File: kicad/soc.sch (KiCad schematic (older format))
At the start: 40 parts, among them J1 Line Out, J2 PS/2 Keyboard, J3 Headphone Out, J4 Line In, P1 LED MATRIX, P2 ALTERA_DE1_GPIO, U1 SSM2603, U2 DS3234

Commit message: start of IO board changes
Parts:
- removed R10, R11: 1k, Resistors_SMD:R_0805_HandSoldering, symbol R
- added D?: PWR, symbol Led_Small
- added P?: IO, symbol CONN_02X04
- added R? (x3): 100K, Resistors_SMD:R_0805_HandSoldering, symbol R
- added R?: 100, Resistors_SMD:R_0805_HandSoldering, symbol R
- added U?: speakjet, symbol speakjet
- C10, C7: footprint Capacitors_ThroughHole:C_Radial_D8_L11.5_P3.5 -> mstock:UWXCAP-6.3mm
- C11, C12, C14, C15: footprint Capacitors_ThroughHole:C_Radial_D5_L6_P2.5 -> mstock:UWXCAP-3mm
- C13, C16, C17, C18: footprint Capacitors_ThroughHole:C_Disc_D3_P2.5 -> Capacitors_SMD:C_0805_HandSoldering
- R3, R6, R7: footprint Resistors_ThroughHole:Resistor_Vertical_RM5mm -> Resistors_SMD:R_0805_HandSoldering
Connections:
- net +3V3: now also R3.1, P?.1 (P1), R?.1, R?.1, R?.1, R?.1, U?.12 (M1), U?.14 (VCC); no longer R3.2
- net GND: now also D?.1 (K), P?.7 (P7), U?.1 (RC1), U?.13 (M0), U?.2 (RC0), U?.3 (E5), U?.4 (E4), U?.5 (Gnd), U?.6 (E3), U?.7 (E2), U?.8 (E1), U?.9 (E0)
- net Kbd_clk: now also J2.5
- net Kbd_data: now also J2.1
- net MISO_33: now also P?.4 (P4)
- net MOSI_33: now also P?.2 (P2)
- net SCLK: now also P?.3 (P3), R?.2
- net SCLK_33: now also P?.6 (P6)
- net SDIN: now also P?.5 (P5), R?.2
- net ~OE: now also R?.2
- net ~RTC_SS: now also P?.8 (P8)
- net MCLK: now reaches P2.31 (IO_A26)
- net MCLK: now also U1.1 (MCLK/XTI)
- net SPEAK: now reaches P2.32 (IO_A27)
- net SPEAK: now also U?.16 (D1)
- net ~RESET: now reaches P2.34 (IO_A29)
- net ~RESET: now also U2.6 (~RST), U?.11 (Reset)
- net at U1.25 (MUTE): now also R3.2; no longer R3.1
- new net: D?.2 (A), R?.2
- new net Serial1_TX: U?.10 (RCX)
- new net Serial1_busy: U?.15 (D2)
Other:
- moved on the sheet: C12, C15, C16, C18, J4, R3

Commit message: more work on new IO board
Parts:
- added R13, R14: 10k, Resistors_SMD:R_0805_HandSoldering, symbol R
- D1: renamed from D?; footprint (none) -> mstock:SM1206POL
- P3: renamed from P?; footprint (none) -> Pin_Headers:Pin_Header_Straight_2x06; symbol CONN_02X04 -> CONN_02X06
- U3: renamed from U?; footprint (none) -> Housings_DIP:DIP-18_W7.62mm
- gave numbers to parts that had none: 4
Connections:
- net Serial1 is gone; now on net Serial1_TX: P2.1 (IO_A0)
- net GND: now also P3.11 (P11); no longer P3.7 (P7)
- net Serial1_TX: now also P3.9 (P9)
- net GPIO1: now reaches P2.33 (IO_A28)
- net GPIO1: now also P3.10 (P10)
- net GPIO2: now reaches P2.35 (IO_A30)
- net GPIO2: now also P3.12 (P12)
- net at U1.16 (LOUT): now also R14.2; no longer C14.1
- net voice: now reaches U3.18 (Voice)
- net voice: now also P3.7 (P7), R13.2
- net SPEAK renamed speaking
- new net: C14.1, R13.1, R14.1
- no-connect marks 10 -> 15
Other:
- moved on the sheet: U3
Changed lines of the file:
@@
 $EndComp
 Text Label 1750 1200 2    60   ~ 0
-Serial1
+Serial1_TX
 $Comp
 L +3.3V #PWR01
@@
 MCLK
 $Comp
-L R R?
+L R R11
 U 1 1 5830728C
 P 3450 4600
-F 0 "R?" V 3243 4600 50  0000 C CNN
+F 0 "R11" V 3243 4600 50  0000 C CNN
 F 1 "100K" V 3334 4600 50  0000 C CNN
 F 2 "Resistors_SMD:R_0805_HandSoldering" V 3380 4600 50  0001 C CNN
@@
 $EndComp
 $Comp
-L R R?
+L R R10
 U 1 1 5830740A
 P 3150 4600
-F 0 "R?" V 2943 4600 50  0000 C CNN
+F 0 "R10" V 2943 4600 50  0000 C CNN
 F 1 "100K" V 3034 4600 50  0000 C CNN
 F 2 "Resistors_SMD:R_0805_HandSoldering" V 3080 4600 50  0001 C CNN
@@
 $EndComp
 $Comp
-L CONN_02X04 P?
+L CONN_02X06 P3
 U 1 1 58308B84
-P 8350 2400
-F 0 "P?" H 8350 2650 50  0000 C CNN
-F 1 "IO" V 8350 2400 50  0000 C CNN
-F 2 "" H 8350 1200 50  0000 C CNN
-F 3 "" H 8350 1200 50  0000 C CNN
-	1    8350 2400
+P 8350 2500
+F 0 "P3" H 8350 2850 50  0000 C CNN
+F 1 "IO" V 8350 2500 50  0000 C CNN
+F 2 "Pin_Headers:Pin_Header_Straight_2x06" H 8350 1300 50  0001 C CNN
+F 3 "" H 8350 1300 50  0000 C CNN
+	1    8350 2500
 	1    0    0    -1
 $EndComp
@@
 ~RTC_SS
 $Comp
-L +3.3V #PWR?
+L +3.3V #PWR021
 U 1 1 583094AC
 P 8100 2150
-F 0 "#PWR?" H 8100 2000 50  0001 C CNN
+F 0 "#PWR021" H 8100 2000 50  0001 C CNN
 F 1 "+3.3V" H 8100 2290 50  0000 C CNN
 F 2 "" H 8100 2150 60  0000 C CNN
@@
 $EndComp
 $Comp
-L GND #PWR?
+L GND #PWR022
 U 1 1 58309716
-P 8100 2650
-F 0 "#PWR?" H 8100 2400 50  0001 C CNN
-F 1 "GND" H 8100 2500 50  0000 C CNN
-F 2 "" H 8100 2650 60  0000 C CNN
-F 3 "" H 8100 2650 60  0000 C CNN
-	1    8100 2650
-	1    0    0    -1
-$EndComp
-$Comp
-L Led_Small D?
+P 8100 2850
+F 0 "#PWR022" H 8100 2600 50  0001 C CNN
+F 1 "GND" H 8100 2700 50  0000 C CNN
+F 2 "" H 8100 2850 60  0000 C CNN
+F 3 "" H 8100 2850 60  0000 C CNN
+	1    8100 2850
+	1    0    0    -1
+$EndComp
+$Comp
+L Led_Small D1
 U 1 1 58309858
 P 9750 2150
-F 0 "D?" H 9750 2385 50  0000 C CNN
+F 0 "D1" H 9750 2385 50  0000 C CNN
 F 1 "PWR" H 9750 2294 50  0000 C CNN
-F 2 "" V 9750 2150 50  0000 C CNN
+F 2 "mstock:SM1206POL" V 9750 2150 50  0001 C CNN
 F 3 "" V 9750 2150 50  0000 C CNN
 	1    9750 2150
@@
 $EndComp
 $Comp
-L +3.3V #PWR?
+L +3.3V #PWR023
 U 1 1 58309B06
 P 10200 2050
-F 0 "#PWR?" H 10200 1900 50  0001 C CNN
+F 0 "#PWR023" H 10200 1900 50  0001 C CNN
 F 1 "+3.3V" H 10200 2190 50  0000 C CNN
 F 2 "" H 10200 2050 60  0000 C CNN
@@
 $EndComp
 $Comp
-L R R?
+L R R15
 U 1 1 58309C0D
 P 10050 2150
-F 0 "R?" V 10130 2150 50  0000 C CNN
+F 0 "R15" V 10130 2150 50  0000 C CNN
 F 1 "100" V 10050 2150 50  0000 C CNN
 F 2 "Resistors_SMD:R_0805_HandSoldering" V 9980 2150 50  0001 C CNN
@@
 $EndComp
 $Comp
-L GND #PWR?
+L GND #PWR024
 U 1 1 58309F9E
 P 9650 2200
-F 0 "#PWR?" H 9650 1950 50  0001 C CNN
+F 0 "#PWR024" H 9650 1950 50  0001 C CNN
 F 1 "GND" H 9650 2050 50  0000 C CNN
 F 2 "" H 9650 2200 60  0000 C CNN
@@
 $EndComp
 $Comp
-L R R?
+L R R12
 U 1 1 5830A3C4
 P 4250 1500
-F 0 "R?" V 4043 1500 50  0000 C CNN
+F 0 "R12" V 4043 1500 50  0000 C CNN
 F 1 "100K" V 4134 1500 50  0000 C CNN
 F 2 "Resistors_SMD:R_0805_HandSoldering" V 4180 1500 50  0001 C CNN
@@
 $EndComp
 $Comp
-L +3.3V #PWR?
+L +3.3V #PWR025
 U 1 1 5830A737
 P 4250 1250
-F 0 "#PWR?" H 4250 1100 50  0001 C CNN
+F 0 "#PWR025" H 4250 1100 50  0001 C CNN
 F 1 "+3.3V" H 4250 1390 50  0000 C CNN
 F 2 "" H 4250 1250 60  0000 C CNN
@@
 $EndComp
 $Comp
-L speakjet U?
+L speakjet U3
 U 1 1 583237DA
-P 3400 6700
-F 0 "U?" H 3425 7347 60  0000 C CNN
-F 1 "speakjet" H 3425 7241 60  0000 C CNN
-F 2 "" H 3450 6650 60  0000 C CNN
-F 3 "" H 3450 6650 60  0000 C CNN
-	1    3400 6700
-	1    0    0    -1
-$EndComp
-$Comp
-L GND #PWR?
+P 1550 4300
+F 0 "U3" H 1575 4947 60  0000 C CNN
+F 1 "speakjet" H 1575 4841 60  0000 C CNN
+F 2 "Housings_DIP:DIP-18_W7.62mm" H 1600 4250 60  0001 C CNN
+F 3 "" H 1600 4250 60  0000 C CNN
+	1    1550 4300
+	1    0    0    -1
+$EndComp
+$Comp
+L GND #PWR026
 U 1 1 583239A7
-P 2900 7200
-F 0 "#PWR?" H 2900 6950 50  0001 C CNN
-F 1 "GND" H 2900 7050 50  0000 C CNN
-F 2 "" H 2900 7200 60  0000 C CNN
-F 3 "" H 2900 7200 60  0000 C CNN
-	1    2900 7200
+P 1050 4800
+F 0 "#PWR026" H 1050 4550 50  0001 C CNN
+F 1 "GND" H 1050 4650 50  0000 C CNN
+F 2 "" H 1050 4800 60  0000 C CNN
+F 3 "" H 1050 4800 60  0000 C CNN
+	1    1050 4800
 	1    0    0    -1
 $EndComp
@@
 Connection ~ 8600 4300
 Wire Wire Line
-	7950 4100 6250 4100
-Wire Wire Line
-	6250 4100 6250 4150
-Wire Wire Line
-	6250 4150 5550 4150
+	5550 4150 6450 4150
 Wire Wire Line
 	5800 4300 7550 4300
@@
 	8100 2150 8100 2250
 Wire Wire Line
-	8100 2550 8100 2650
-Wire Wire Line
 	10200 2050 10200 2150
 Wire Wire Line
@@
 	4250 1250 4250 1350
 Wire Wire Line
-	2950 7100 2900 7100
-Wire Wire Line
-	2900 6300 2900 7200
-Wire Wire Line
-	2950 7000 2900 7000
-Connection ~ 2900 7100
-Wire Wire Line
-	2950 6900 2900 6900
-Connection ~ 2900 7000
-Wire Wire Line
-	2950 6800 2900 6800
-Connection ~ 2900 6900
-Wire Wire Line
-	2950 6700 2900 6700
-Connection ~ 2900 6800
-Wire Wire Line
-	2950 6300 2900 6300
-Connection ~ 2900 6700
-Wire Wire Line
-	2950 6600 2900 6600
-Connection ~ 2900 6600
-Wire Wire Line
-	2950 6500 2900 6500
-Connection ~ 2900 6500
-Wire Wire Line
-	2950 6400 2900 6400
-Connection ~ 2900 6400
-Text Label 3900 7100 0    60   ~ 0
+	1100 4700 1050 4700
+Wire Wire Line
+	1050 3900 1050 4800
+Wire Wire Line
+	1100 4600 1050 4600
+Connection ~ 1050 4700
+Wire Wire Line
+	1100 4500 1050 4500
+Connection ~ 1050 4600
+Wire Wire Line
+	1100 4400 1050 4400
+Connection ~ 1050 4500
+Wire Wire Line
+	1100 4300 1050 4300
+Connection ~ 1050 4400
+Wire Wire Line
+	1100 3900 1050 3900
+Connection ~ 1050 4300
+Wire Wire Line
+	1100 4200 1050 4200
+Connection ~ 1050 4200
+Wire Wire Line
+	1100 4100 1050 4100
+Connection ~ 1050 4100
+Wire Wire Line
+	1100 4000 1050 4000
+Connection ~ 1050 4000
+Text Label 2050 4700 0    60   ~ 0
 Serial1_TX
 $Comp
-L +3.3V #PWR?
+L +3.3V #PWR027
 U 1 1 58324642
-P 4500 6400
-F 0 "#PWR?" H 4500 6250 50  0001 C CNN
-F 1 "+3.3V" H 4500 6540 50  0000 C CNN
-F 2 "" H 4500 6400 60  0000 C CNN
-F 3 "" H 4500 6400 60  0000 C CNN
-	1    4500 6400
-	1    0    0    -1
-$EndComp
-Wire Wire Line
-	3900 6900 4500 6900
-$Comp
-L GND #PWR?
+P 2650 4000
+F 0 "#PWR027" H 2650 3850 50  0001 C CNN
+F 1 "+3.3V" H 2650 4140 50  0000 C CNN
+F 2 "" H 2650 4000 60  0000 C CNN
+F 3 "" H 2650 4000 60  0000 C CNN
+	1    2650 4000
+	1    0    0    -1
+$EndComp
+Wire Wire Line
+	2050 4500 2650 4500
+$Comp
+L GND #PWR028
 U 1 1 58324B78
-P 4450 7200
-F 0 "#PWR?" H 4450 6950 50  0001 C CNN
-F 1 "GND" H 4450 7050 50  0000 C CNN
-F 2 "" H 4450 7200 60  0000 C CNN
-F 3 "" H 4450 7200 60  0000 C CNN
-	1    4450 7200
-	1    0    0    -1
-$EndComp
-Wire Wire Line
-	3900 6800 4450 6800
-Text Label 2750 2700 0    60   ~ 0
-SPEAK
-Text Label 3900 6500 0    60   ~ 0
-SPEAK
-Wire Wire Line
-	3900 6700 4500 6700
+P 2600 4800
+F 0 "#PWR028" H 2600 4550 50  0001 C CNN
+F 1 "GND" H 2600 4650 50  0000 C CNN
+F 2 "" H 2600 4800 60  0000 C CNN
+F 3 "" H 2600 4800 60  0000 C CNN
+	1    2600 4800
+	1    0    0    -1
+$EndComp
+Wire Wire Line
+	2050 4400 2600 4400
+Text Label 2050 4100 0    60   ~ 0
+speaking
+Wire Wire Line
+	2050 4300 2650 4300
 Text Label 2750 2800 0    60   ~ 0
 ~RESET
-Text Label 3900 7000 0    60   ~ 0
+Text Label 2050 4600 0    60   ~ 0
 ~RESET
 Text Label 6100 1400 2    60   ~ 0
 ~RESET
-NoConn ~ 3900 6400
-Wire Wire Line
-	4450 6800 4450 7200
-Text Label 3900 6600 0    60   ~ 0
+NoConn ~ 2050 4000
+Wire Wire Line
+	2600 4400 2600 4800
+Text Label 2050 4200 0    60   ~ 0
 Serial1_busy
 Wire Wire Line
-	4500 6900 4500 6400
-Connection ~ 4500 6700
+	2650 4500 2650 4000
+Connection ~ 2650 4300
+Text Label 2750 2700 0    60   ~ 0
+speaking
+Text Label 2050 3900 0    60   ~ 0
+voice
+Text Label 6450 3800 2    60   ~ 0
+voice
+$Comp
+L R R13
+U 1 1 583306F5
+P 6600 3800
+F 0 "R13" V 6680 3800 50  0000 C CNN
+F 1 "10k" V 6600 3800 50  0000 C CNN
+F 2 "Resistors_SMD:R_0805_HandSoldering" V 6530 3800 50  0001 C CNN
+F 3 "" H 6600 3800 50  0000 C CNN
+	1    6600 3800
+	0    1    1    0
+$EndComp
+$Comp
+L R R14
+U 1 1 583307D9
+P 6600 4100
+F 0 "R14" V 6680 4100 50  0000 C CNN
+F 1 "10k" V 6600 4100 50  0000 C CNN
+F 2 "Resistors_SMD:R_0805_HandSoldering" V 6530 4100 50  0001 C CNN
+F 3 "" H 6600 4100 50  0000 C CNN
+	1    6600 4100
+	0    1    1    0
+$EndComp
+Wire Wire Line
+	6450 4150 6450 4100
+Wire Wire Line
+	6750 3800 6750 4100
+Wire Wire Line
+	6750 4100 7950 4100
+Connection ~ 6750 4100
+Wire Wire Line
+	8100 2750 8100 2850
+Text Label 8100 2550 2    60   ~ 0
+voice
+Text Label 8100 2650 2    60   ~ 0
+Serial1_TX
+Text Label 1750 2800 2    60   ~ 0
+GPIO1
+Text Label 1750 2900 2    60   ~ 0
+GPIO2
+Text Label 8600 2750 0    60   ~ 0
+GPIO2
+Text Label 8600 2650 0    60   ~ 0
+GPIO1
+NoConn ~ 2750 2900
+NoConn ~ 2750 3000
+NoConn ~ 2750 3100
+NoConn ~ 1750 3000
+NoConn ~ 1750 3100
 $EndSCHEMATC

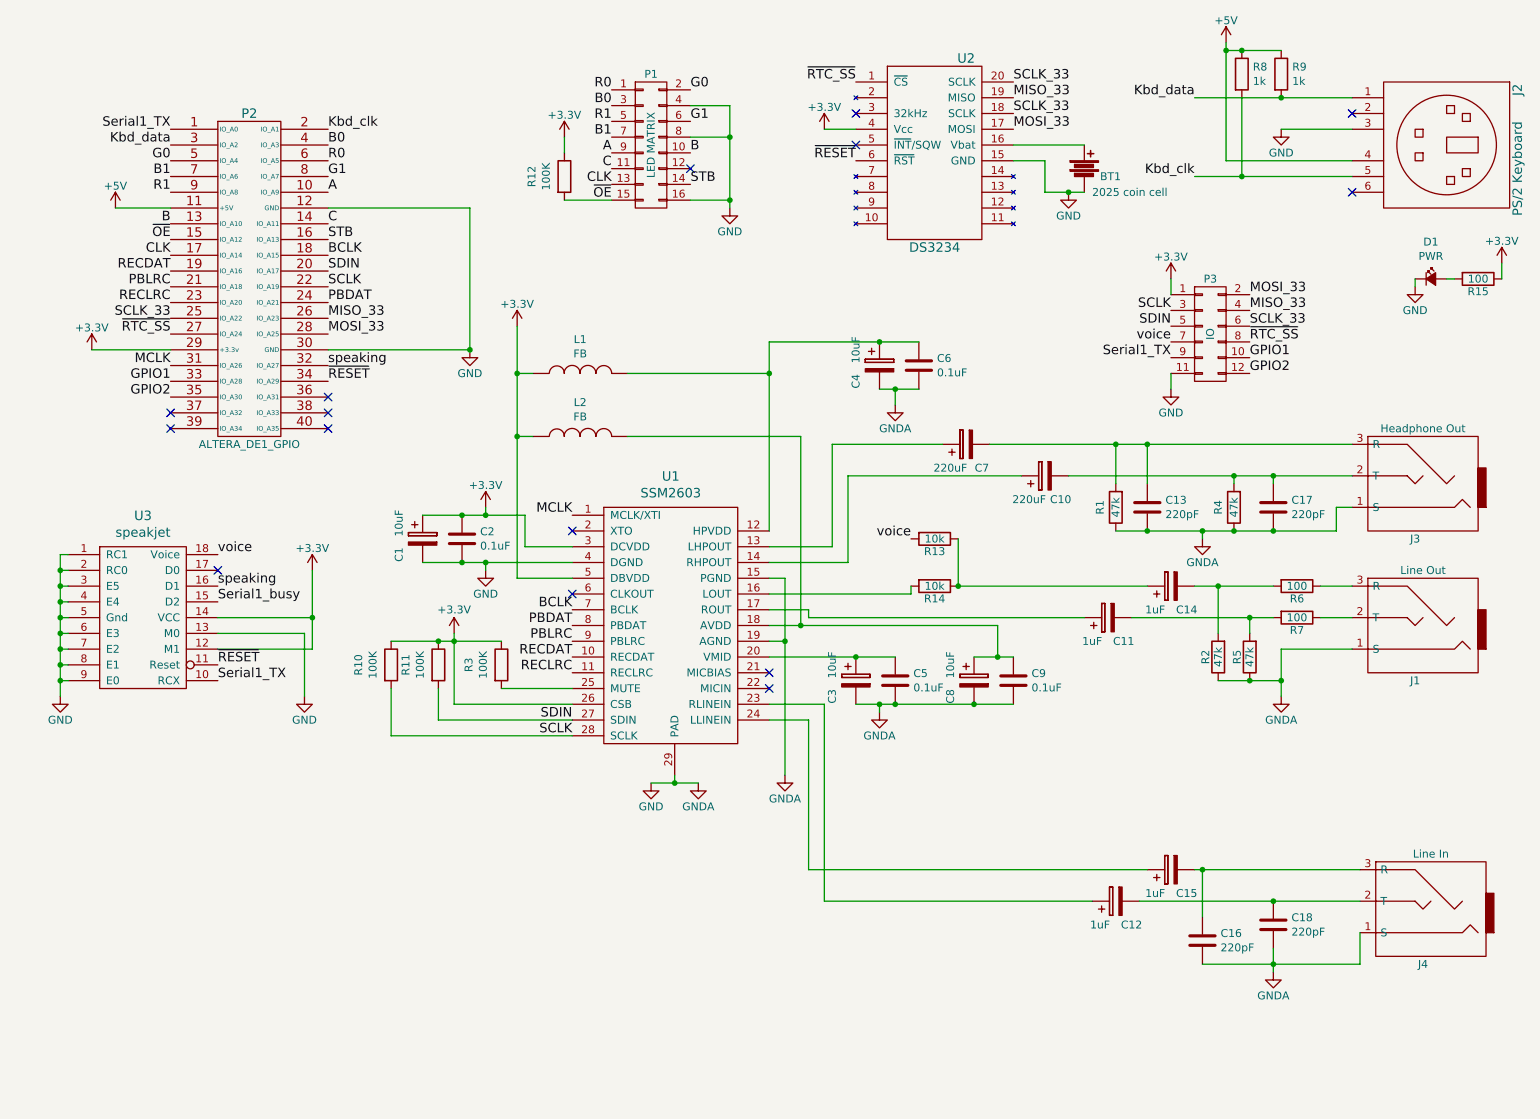
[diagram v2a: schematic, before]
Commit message: add level converter and start to add mic input
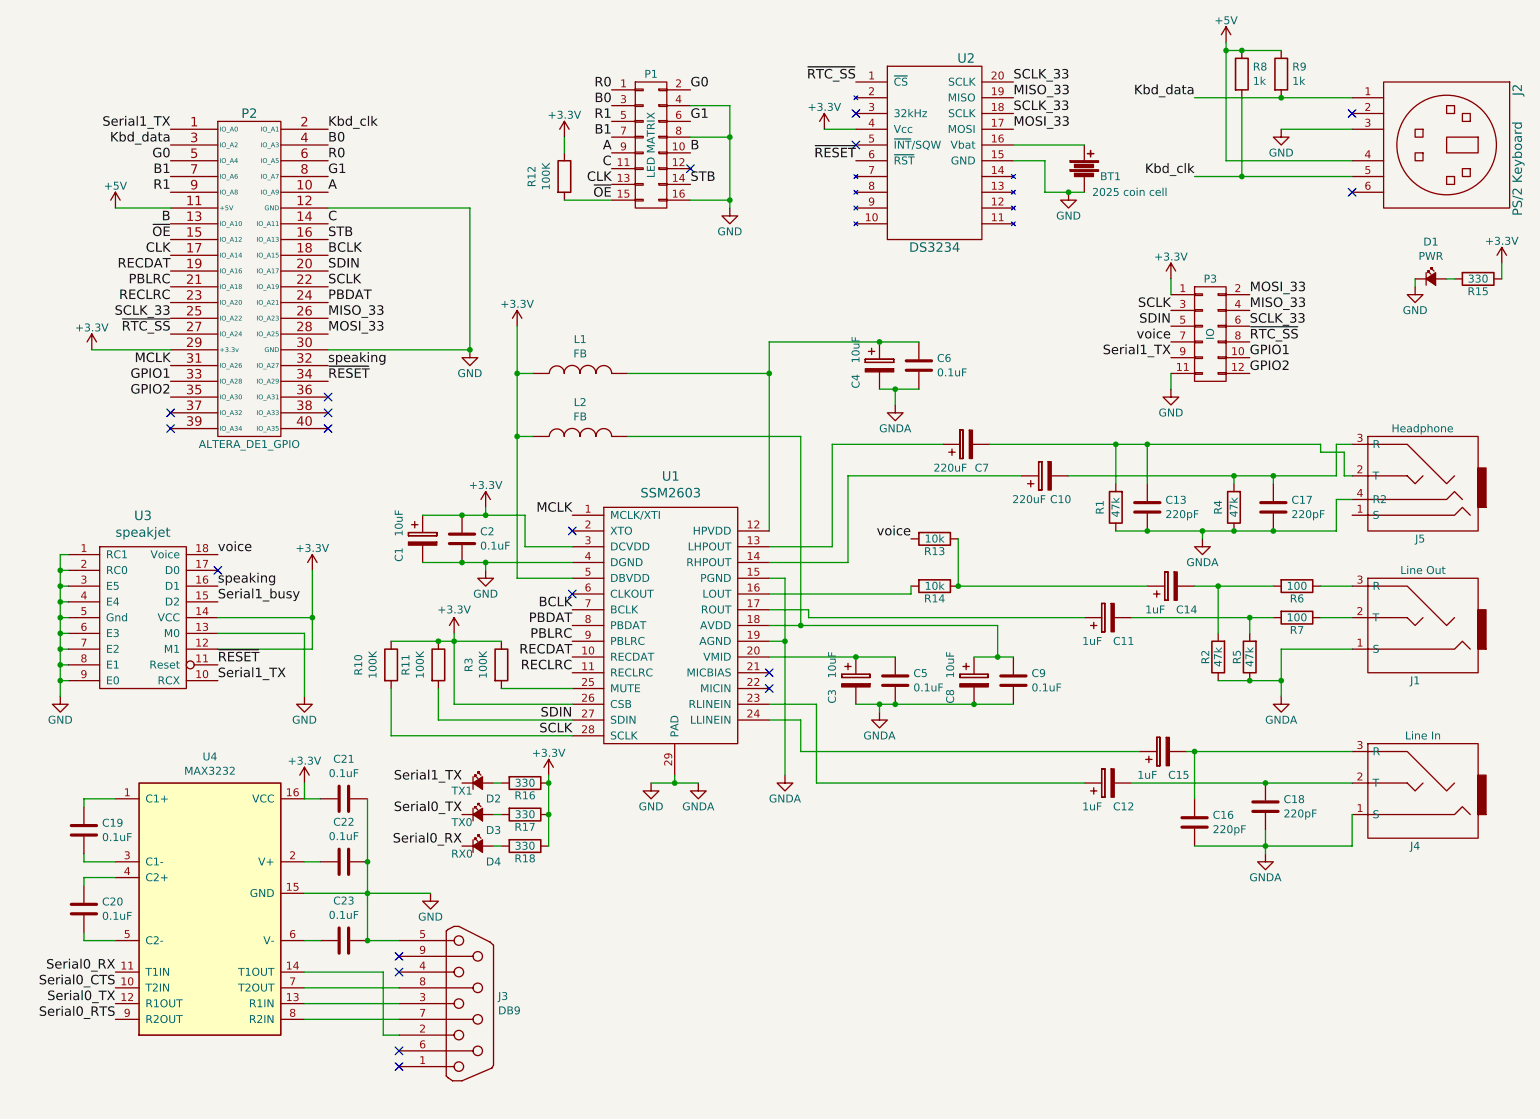
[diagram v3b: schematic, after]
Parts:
- removed J3: Headphone Out, mstock-pretty:SJI-3513N, symbol JACK_TRS_3PINS
- added C19, C20, C21, C22, C23: 0.1uF, Capacitors_SMD:C_0805_HandSoldering, symbol C
- added D2: TX1, mstock:SM1206POL, symbol Led_Small
- added D3: TX0, mstock:SM1206POL, symbol Led_Small
- added D4: RX0, mstock:SM1206POL, symbol Led_Small
- added J3: DB9, symbol DB9
- added J5: Headphone, symbol JACK_TRRS_4PINS
- added R16, R17, R18: 330, Resistors_SMD:R_0805_HandSoldering, symbol R
- added U4: MAX3232, symbol MAX3232
- R15: value 100 -> 330
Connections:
- net +3V3: now also C21.1, R16.1, R17.1, R18.1, U4.16 (VCC)
- net GND: now also C21.2, C22.1, C23.1, J3.5, J5.4 (R2), U4.15 (GND)
- net Serial1_TX: now also D2.1 (K)
- net at C13.2, C7.2, R1.2: now also J5.2 (T)
- net at C10.2, C17.2, R4.2: now also J5.3 (R)
- new net: C19.1, U4.1 (C1+)
- new net: J3.3, U4.13 (R1IN)
- new net: J3.2, U4.14 (T1OUT)
- new net: C22.2, U4.2 (V+)
- new net: C19.2, U4.3 (C1-)
- new net: C20.1, U4.4 (C2+)
- new net: C20.2, U4.5 (C2-)
- new net: C23.2, U4.6 (V-)
- new net: J3.8 (P8), U4.7 (T2OUT)
- new net: J3.7 (P7), U4.8 (R2IN)
- new net: D3.2 (A), R17.2
- new net: D2.2 (A), R16.2
- new net: D4.2 (A), R18.2
- new net Serial0_CTS: U4.10 (T2IN)
- new net Serial0_RTS: U4.9 (R2OUT)
- new net Serial0_RX: D4.1 (K), U4.11 (T1IN)
- new net Serial0_TX: D3.1 (K), U4.12 (R1OUT)
- no-connect marks 15 -> 19
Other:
- moved on the sheet: C12, C15, C16, C18, J4
